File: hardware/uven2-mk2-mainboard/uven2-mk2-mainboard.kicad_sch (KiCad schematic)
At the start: 7 parts, among them U1 DEV-16771, U2 MCP48FEB28T-20E/ST, U3 MCP48FEB28T-20E/ST

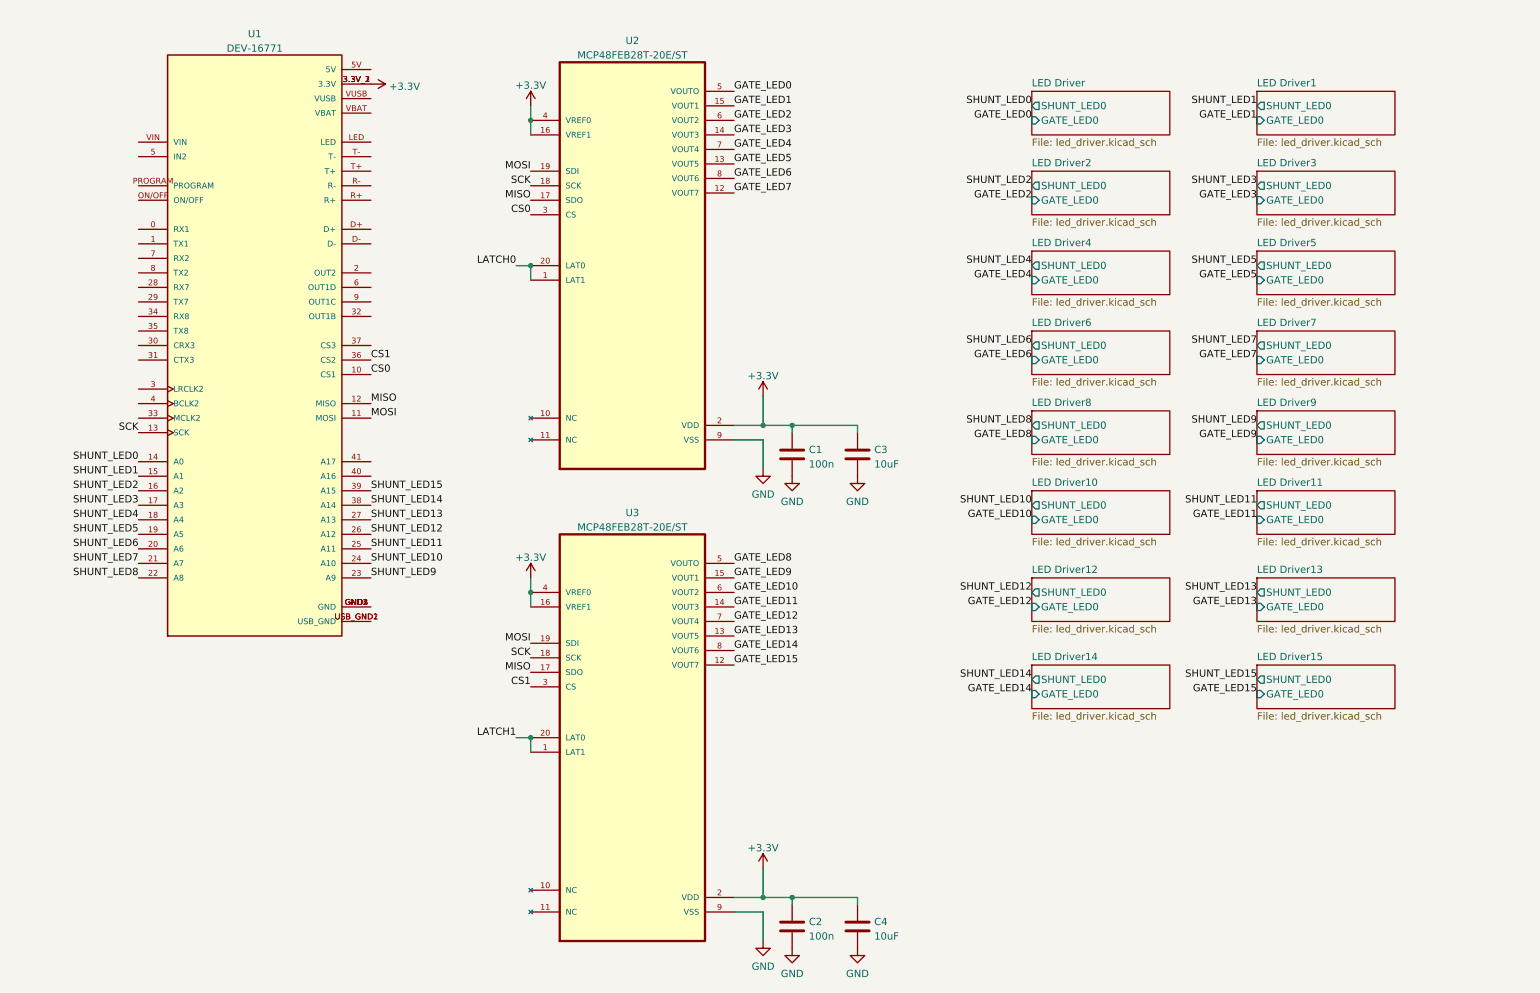
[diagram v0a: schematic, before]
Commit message: with current limiting switch
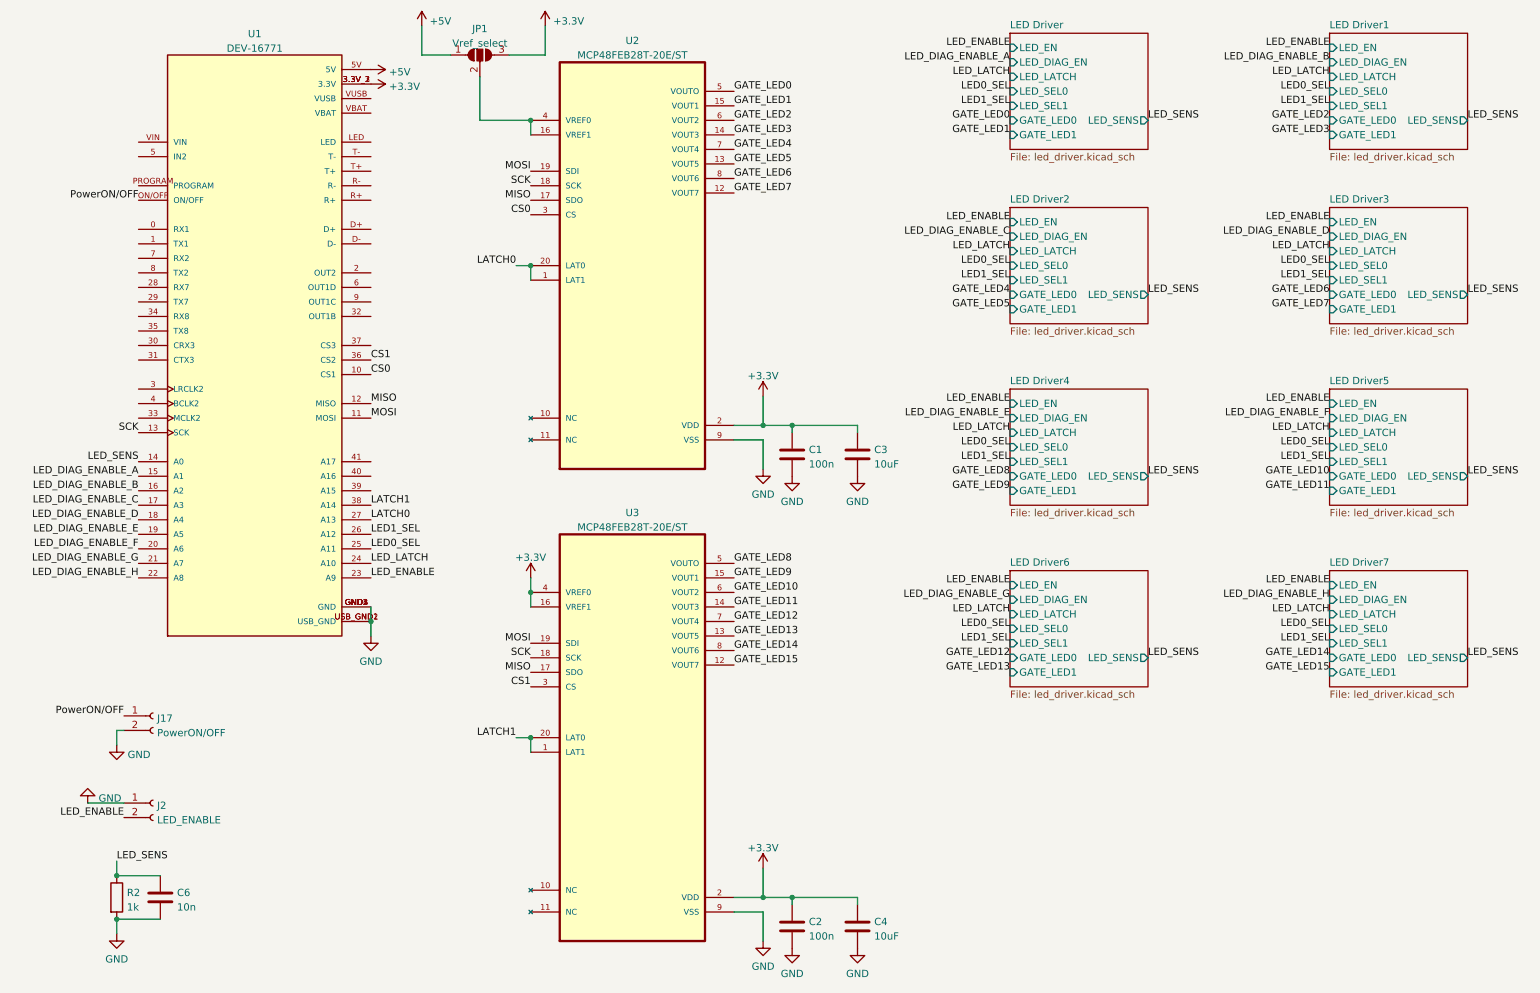
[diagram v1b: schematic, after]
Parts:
- added C6: 10n, Capacitor_SMD:C_0603_1608Metric_Pad1.08x0.95mm_HandSolder, symbol Device:C
- added J17: PowerON/OFF, Connector_PinHeader_2.54mm:PinHeader_1x02_P2.54mm_Vertical, symbol Connector:Conn_01x02_Female
- added J2: LED_ENABLE, Connector_PinHeader_2.54mm:PinHeader_1x02_P2.54mm_Vertical, symbol Connector:Conn_01x02_Female
- added JP1: Vref_select, Jumper:SolderJumper-3_P1.3mm_Open_RoundedPad1.0x1.5mm_NumberLabels, symbol Jumper:SolderJumper_3_Open
- added R2: 1k, Resistor_SMD:R_0603_1608Metric_Pad0.98x0.95mm_HandSolder, symbol Device:R
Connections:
- net SHUNT_LED13 is gone; now on net LATCH0: U1.27 (A13)
- net SHUNT_LED14 is gone; now on net LATCH1: U1.38 (A14)
- net +3.3V: now also JP1.3 (B); no longer U2.16 (VREF1), U2.4 (VREF0)
- net GND: now also U1.GND1 (GND), U1.GND2 (GND), U1.GND3 (GND), U1.GND4 (GND), U1.GND5 (GND), U1.USB_GND1 (USB_GND), U1.USB_GND2 (USB_GND), C6.2, J17.2 (Pin_2), J2.1 (Pin_1), R2.2
- net +5V: now reaches U1.5V
- net +5V: now also JP1.1 (A)
- net PowerON/OFF: now reaches U1.ON/OFF
- net PowerON/OFF: now also J17.1 (Pin_1)
- net SHUNT_LED0 renamed LED_SENS
- net LED_SENS: now also C6.1, R2.1
- net SHUNT_LED1 renamed LED_DIAG_ENABLE_A
- net SHUNT_LED10 renamed LED_LATCH
- net SHUNT_LED11 renamed LED0_SEL
- net SHUNT_LED12 renamed LED1_SEL
- net SHUNT_LED15: no longer names the net of U1.39 (A15)
- net SHUNT_LED2 renamed LED_DIAG_ENABLE_B
- net SHUNT_LED3 renamed LED_DIAG_ENABLE_C
- net SHUNT_LED4 renamed LED_DIAG_ENABLE_D
- net SHUNT_LED5 renamed LED_DIAG_ENABLE_E
- net SHUNT_LED6 renamed LED_DIAG_ENABLE_F
- net SHUNT_LED7 renamed LED_DIAG_ENABLE_G
- net SHUNT_LED8 renamed LED_DIAG_ENABLE_H
- net SHUNT_LED9 renamed LED_ENABLE
- net LED_ENABLE: now also J2.2 (Pin_2)
- new net: JP1.2 (C), U2.16 (VREF1), U2.4 (VREF0)
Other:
- removed sheet LED Driver10
- removed sheet LED Driver11
- removed sheet LED Driver12
- removed sheet LED Driver13
- removed sheet LED Driver14
- removed sheet LED Driver15
- removed sheet LED Driver8
- removed sheet LED Driver9
- sheet LED Driver ports: added GATE_LED1, LED_DIAG_EN, LED_EN, LED_LATCH, LED_SEL0, LED_SEL1, LED_SENS; removed SHUNT_LED0
- sheet LED Driver1 ports: added GATE_LED1, LED_DIAG_EN, LED_EN, LED_LATCH, LED_SEL0, LED_SEL1, LED_SENS; removed SHUNT_LED0
- sheet LED Driver2 ports: added GATE_LED1, LED_DIAG_EN, LED_EN, LED_LATCH, LED_SEL0, LED_SEL1, LED_SENS; removed SHUNT_LED0
- sheet LED Driver3 ports: added GATE_LED1, LED_DIAG_EN, LED_EN, LED_LATCH, LED_SEL0, LED_SEL1, LED_SENS; removed SHUNT_LED0
- sheet LED Driver4 ports: added GATE_LED1, LED_DIAG_EN, LED_EN, LED_LATCH, LED_SEL0, LED_SEL1, LED_SENS; removed SHUNT_LED0
- sheet LED Driver5 ports: added GATE_LED1, LED_DIAG_EN, LED_EN, LED_LATCH, LED_SEL0, LED_SEL1, LED_SENS; removed SHUNT_LED0
- sheet LED Driver6 ports: added GATE_LED1, LED_DIAG_EN, LED_EN, LED_LATCH, LED_SEL0, LED_SEL1, LED_SENS; removed SHUNT_LED0
- sheet LED Driver7 ports: added GATE_LED1, LED_DIAG_EN, LED_EN, LED_LATCH, LED_SEL0, LED_SEL1, LED_SENS; removed SHUNT_LED0

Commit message: with wago connector
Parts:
- added J1: 713-1436_037-000, custom_lib:CONN_713-1436&slash_037-000_WAG, symbol 713-1436_037-000:713-1436_037-000
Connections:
- net LATCH0: now also U1.6 (OUT1D); no longer U1.27 (A13)
- net LATCH1: now also U1.7 (RX2); no longer U1.38 (A14)
- net LED0_SEL: now also U1.4 (BCLK2); no longer U1.25 (A11)
- net LED1_SEL: now also U1.5 (IN2); no longer U1.26 (A12)
- net LED_DIAG_ENABLE_A: now also U1.8 (TX2); no longer U1.15 (A1)
- net LED_DIAG_ENABLE_B: now also U1.9 (OUT1C); no longer U1.16 (A2)
- net LED_DIAG_ENABLE_C: now also U1.28 (RX7); no longer U1.17 (A3)
- net LED_DIAG_ENABLE_D: now also U1.29 (TX7); no longer U1.18 (A4)
- net LED_DIAG_ENABLE_E: now also U1.30 (CRX3); no longer U1.19 (A5)
- net LED_DIAG_ENABLE_F: now also U1.31 (CTX3); no longer U1.20 (A6)
- net LED_DIAG_ENABLE_G: now also U1.33 (MCLK2); no longer U1.21 (A7)
- net LED_DIAG_ENABLE_H: now also U1.34 (RX8); no longer U1.22 (A8)
- net LED_ENABLE: now also U1.2 (OUT2); no longer U1.23 (A9)
- net LED_LATCH: now also U1.3 (LRCLK2); no longer U1.24 (A10)
- net TEMP_LED14: now reaches U1.39 (A15)
- net TEMP_LED15: now reaches U1.40 (A16)
- new net LED0+: J1.2
- new net LED0-: J1.1
- new net LED1+: J1.4
- new net LED1-: J1.3
- new net LED10+: J1.22
- new net LED10-: J1.21
- new net LED11+: J1.24
- new net LED11-: J1.23
- new net LED12+: J1.26
- new net LED12-: J1.25
- new net LED13+: J1.28
- new net LED13-: J1.27
- new net LED14+: J1.30
- new net LED14-: J1.29
- new net LED15+: J1.32
- new net LED15-: J1.31
- new net LED2+: J1.6
- new net LED2-: J1.5
- new net LED3+: J1.8
- new net LED3-: J1.7
- new net LED4+: J1.10
- new net LED4-: J1.9
- new net LED5+: J1.12
- new net LED5-: J1.11
- new net LED6+: J1.14
- new net LED6-: J1.13
- new net LED7+: J1.16
- new net LED7-: J1.15
- new net LED8+: J1.18
- new net LED8-: J1.17
- new net LED9+: J1.20
- new net LED9-: J1.19
- new net TEMP_LED0: U1.15 (A1)
- new net TEMP_LED1: U1.16 (A2)
- new net TEMP_LED10: U1.25 (A11)
- new net TEMP_LED11: U1.26 (A12)
- new net TEMP_LED12: U1.27 (A13)
- new net TEMP_LED13: U1.38 (A14)
- new net TEMP_LED2: U1.17 (A3)
- new net TEMP_LED3: U1.18 (A4)
- new net TEMP_LED4: U1.19 (A5)
- new net TEMP_LED5: U1.20 (A6)
- new net TEMP_LED6: U1.21 (A7)
- new net TEMP_LED7: U1.22 (A8)
- new net TEMP_LED8: U1.23 (A9)
- new net TEMP_LED9: U1.24 (A10)
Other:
- sheet LED Driver ports: added LED0+, LED0-, LED1+, LED1-, TEMP_LED0, TEMP_LED1; removed none
- sheet LED Driver1 ports: added LED0+, LED0-, LED1+, LED1-, TEMP_LED0, TEMP_LED1; removed none
- sheet LED Driver2 ports: added LED0+, LED0-, LED1+, LED1-, TEMP_LED0, TEMP_LED1; removed none
- sheet LED Driver3 ports: added LED0+, LED0-, LED1+, LED1-, TEMP_LED0, TEMP_LED1; removed none
- sheet LED Driver4 ports: added LED0+, LED0-, LED1+, LED1-, TEMP_LED0, TEMP_LED1; removed none
- sheet LED Driver5 ports: added LED0+, LED0-, LED1+, LED1-, TEMP_LED0, TEMP_LED1; removed none
- sheet LED Driver6 ports: added LED0+, LED0-, LED1+, LED1-, TEMP_LED0, TEMP_LED1; removed none
- sheet LED Driver7 ports: added LED0+, LED0-, LED1+, LED1-, TEMP_LED0, TEMP_LED1; removed none

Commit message: with chamber control
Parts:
- added C?: 100n, Capacitor_SMD:C_0603_1608Metric_Pad1.08x0.95mm_HandSolder, symbol Device:C
- added J?: J1B1211CCD, J1B1211CCD, symbol J1B1211CCD:J1B1211CCD
- added J? (x5): GND, symbol Connector:Conn_01x01_Female
- added J?: 28V, symbol Connector:Conn_01x01_Female
- added J? (x3): 24V, symbol Connector:Conn_01x01_Female
- added J?: 5V, symbol Connector:Conn_01x01_Female
- added J?: LED_CHAMBER_CONTROL, symbol Connector:DB25_Male_MountingHoles
- added JP?: Vref_select, Jumper:SolderJumper-3_P1.3mm_Open_RoundedPad1.0x1.5mm_NumberLabels, symbol Jumper:SolderJumper_3_Open
- added R? (x2): 1k, Resistor_SMD:R_0603_1608Metric_Pad0.98x0.95mm_HandSolder, symbol Device:R
- added U? (x2): G3VM-31DR_TR05_, symbol G3VM-31DR_TR05_:G3VM-31DR_TR05_
- J1: value 713-1436_037-000 -> LEDs
- U2, U3: footprint custom_lib:SOP65P640X120-20N -> SOP65P640X120-20N
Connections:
- net +3.3V: now also JP?.3 (B); no longer U3.16 (VREF1), U3.4 (VREF0)
- net +5V: now also J?.1 (Pin_1), JP?.1 (A)
- net CS0: now also U1.37 (CS3); no longer U1.10 (CS1)
- net GND: now also C?.2, J?.0 (PAD), J?.1 (Pin_1), J?.1 (Pin_1), J?.1 (Pin_1), J?.1 (Pin_1), J?.1 (Pin_1), J?.17 (P17), J?.19 (P19), J?.8 (RGND), J?.9 (KG), U?.2 (K), U?.2 (K), U?.4 (D), U?.4 (D)
- net LED_ENABLE: now also J?.18 (P18)
- net TEMP_LED0: now also J?.1
- net TEMP_LED1: now also J?.2
- net TEMP_LED10: now also J?.11
- net TEMP_LED11: now also J?.12
- net TEMP_LED12: now also J?.13
- net TEMP_LED13: now also J?.14 (P14)
- net TEMP_LED14: now also J?.15 (P15)
- net TEMP_LED15: now also J?.16 (P16)
- net TEMP_LED2: now also J?.3
- net TEMP_LED3: now also J?.4
- net TEMP_LED4: now also J?.5
- net TEMP_LED5: now also J?.6
- net TEMP_LED6: now also J?.7
- net TEMP_LED7: now also J?.8
- net TEMP_LED8: now also J?.9
- net TEMP_LED9: now also J?.10
- net at U3.10 (NC): now also U3.11 (NC)
- net LED_FAN: now reaches U1.41 (A17)
- net LED_FAN: now also R?.1
- net ETH_LED: now reaches U1.LED
- net ETH_LED: now also J?.10 (AG)
- net ETH_RX+: now reaches U1.R+
- net ETH_RX+: now also J?.4 (RD+)
- net ETH_RX-: now reaches U1.R-
- net ETH_RX-: now also J?.6 (RD-)
- net ETH_TX+: now reaches U1.T+
- net ETH_TX+: now also J?.1 (TD+)
- net ETH_TX-: now reaches U1.T-
- net ETH_TX-: now also J?.3 (TD-)
- net at U2.10 (NC): now also U2.11 (NC)
- new net: C?.1, J?.2 (TCT), J?.5 (RCT)
- new net: R?.2, U?.1 (A) (x2)
- new net: J?.22 (P22), J?.23 (P23), U?.3 (D2)
- new net: JP?.2 (C), U3.16 (VREF1), U3.4 (VREF0)
- new net: J?.20 (P20), U?.3 (D2)
- new net +24V: J?.1 (Pin_1), J?.1 (Pin_1), J?.1 (Pin_1)
- new net +28V: J?.1 (Pin_1), J?.21 (P21), J?.24 (P24), J?.25 (P25)
- new net CHAMBER_FAN: R?.1
- no-connect marks 0 -> 5
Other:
- moved on the sheet: C1, C2, C3, C4, C6, J1, J17, J2, JP1, R2

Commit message: schematics done
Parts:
- removed J2: LED_ENABLE, Connector_PinHeader_2.54mm:PinHeader_1x02_P2.54mm_Vertical, symbol Connector:Conn_01x02_Female
- removed J? (x2): GND, symbol Connector:Conn_01x01_Female
- removed J?: 28V, symbol Connector:Conn_01x01_Female
- removed J?: 5V, symbol Connector:Conn_01x01_Female
- removed J?: LED_CHAMBER_CONTROL, symbol Connector:DB25_Male_MountingHoles
- removed R? (x2): 1k, Resistor_SMD:R_0603_1608Metric_Pad0.98x0.95mm_HandSolder, symbol Device:R
- removed U? (x2): G3VM-31DR_TR05_, symbol G3VM-31DR_TR05_:G3VM-31DR_TR05_
- added J15: Chamber_Control, Connector_Dsub:DSUB-37_Female_Horizontal_P2.77x2.84mm_EdgePinOffset7.70mm_Housed_MountingHolesOffset9.12mm, symbol Connector:DB37_Male_MountingHoles
- added J2: 1-282834-0, custom_lib:TE_1-282834-0, symbol 1-282834-0:1-282834-0
- added J3: 5V, custom_lib:KEYSTONE_7767, symbol 7767:7767
- added J4, J7: GND, custom_lib:KEYSTONE_7767, symbol 7767:7767
- added J6: 24V, custom_lib:KEYSTONE_7767, symbol 7767:7767
- added J8: USB_HOST, Connector_PinHeader_2.54mm:PinHeader_1x05_P2.54mm_Vertical, symbol Connector:Conn_01x05_Male
- added Q1, Q2: 2N7002, Package_TO_SOT_SMD:SOT-23, symbol Transistor_FET:2N7002
- added R50: 1k, Resistor_SMD:R_0603_1608Metric_Pad0.98x0.95mm_HandSolder, symbol Device:R
- added R51, R52: 10k, Resistor_SMD:R_0603_1608Metric_Pad0.98x0.95mm_HandSolder, symbol Device:R
- added TP1: 5V, custom_lib:TP420X150, symbol RCWCTE:RCWCTE
- added TP10: LED_DIAG_ENABLE_E, custom_lib:TP420X150, symbol RCWCTE:RCWCTE
- added TP11: LED_DIAG_ENABLE_F, custom_lib:TP420X150, symbol RCWCTE:RCWCTE
- added TP12: LED_LATCH, custom_lib:TP420X150, symbol RCWCTE:RCWCTE
- added TP13: LED0_SEL, custom_lib:TP420X150, symbol RCWCTE:RCWCTE
- added TP14: LED_DIAG_ENABLE_G, custom_lib:TP420X150, symbol RCWCTE:RCWCTE
- added TP15: SCK, custom_lib:TP420X150, symbol RCWCTE:RCWCTE
- added TP16: LED_SENS, custom_lib:TP420X150, symbol RCWCTE:RCWCTE
- added TP17: TEMP_LED0, custom_lib:TP420X150, symbol RCWCTE:RCWCTE
- added TP18: TEMP_LED1, custom_lib:TP420X150, symbol RCWCTE:RCWCTE
- added TP19: TEMP_LED2, custom_lib:TP420X150, symbol RCWCTE:RCWCTE
- added TP2, TP26, TP28: GND, custom_lib:TP420X150, symbol RCWCTE:RCWCTE
- added TP20: TEMP_LED3, custom_lib:TP420X150, symbol RCWCTE:RCWCTE
- added TP21: TEMP_LED4, custom_lib:TP420X150, symbol RCWCTE:RCWCTE
- added TP22: TEMP_LED5, custom_lib:TP420X150, symbol RCWCTE:RCWCTE
- added TP23: TEMP_LED6, custom_lib:TP420X150, symbol RCWCTE:RCWCTE
- added TP24: TEMP_LED7, custom_lib:TP420X150, symbol RCWCTE:RCWCTE
- added TP25: 24V_FANS, custom_lib:TP420X150, symbol RCWCTE:RCWCTE
- added TP27: 24V_LEDS, custom_lib:TP420X150, symbol RCWCTE:RCWCTE
- added TP29: LED_ENABLE, custom_lib:TP420X150, symbol RCWCTE:RCWCTE
- added TP3: LED1_SEL, custom_lib:TP420X150, symbol RCWCTE:RCWCTE
- added TP30: LATCH0, custom_lib:TP420X150, symbol RCWCTE:RCWCTE
- added TP31: LED_DIAG_ENABLE_B, custom_lib:TP420X150, symbol RCWCTE:RCWCTE
- added TP32: LED_DIAG_ENABLE_D, custom_lib:TP420X150, symbol RCWCTE:RCWCTE
- added TP33: CS0, custom_lib:TP420X150, symbol RCWCTE:RCWCTE
- added TP34: CS1, custom_lib:TP420X150, symbol RCWCTE:RCWCTE
- added TP35: MISO, custom_lib:TP420X150, symbol RCWCTE:RCWCTE
- added TP36: MOSI, custom_lib:TP420X150, symbol RCWCTE:RCWCTE
- added TP37: LED_DIAG_ENABLE_C, custom_lib:TP420X150, symbol RCWCTE:RCWCTE
- added TP38: TEMP_LED15, custom_lib:TP420X150, symbol RCWCTE:RCWCTE
- added TP39: TEMP_LED14, custom_lib:TP420X150, symbol RCWCTE:RCWCTE
- added TP4: PowerON/OFF, custom_lib:TP420X150, symbol RCWCTE:RCWCTE
- added TP40: TEMP_LED13, custom_lib:TP420X150, symbol RCWCTE:RCWCTE
- added TP41: TEMP_LED12, custom_lib:TP420X150, symbol RCWCTE:RCWCTE
- added TP42: TEMP_LED11, custom_lib:TP420X150, symbol RCWCTE:RCWCTE
- added TP43: TEMP_LED10, custom_lib:TP420X150, symbol RCWCTE:RCWCTE
- added TP44: TEMP_LED9, custom_lib:TP420X150, symbol RCWCTE:RCWCTE
- added TP45: TEMP_LED8, custom_lib:TP420X150, symbol RCWCTE:RCWCTE
- added TP46: GATE_LED0, custom_lib:TP420X150, symbol RCWCTE:RCWCTE
- added TP47: GATE_LED1, custom_lib:TP420X150, symbol RCWCTE:RCWCTE
- added TP48: GATE_LED2, custom_lib:TP420X150, symbol RCWCTE:RCWCTE
- added TP49: GATE_LED3, custom_lib:TP420X150, symbol RCWCTE:RCWCTE
- added TP5: LATCH1, custom_lib:TP420X150, symbol RCWCTE:RCWCTE
- added TP50: GATE_LED4, custom_lib:TP420X150, symbol RCWCTE:RCWCTE
- added TP51: GATE_LED5, custom_lib:TP420X150, symbol RCWCTE:RCWCTE
- added TP52: GATE_LED6, custom_lib:TP420X150, symbol RCWCTE:RCWCTE
- added TP53: GATE_LED7, custom_lib:TP420X150, symbol RCWCTE:RCWCTE
- added TP54: GATE_LED8, custom_lib:TP420X150, symbol RCWCTE:RCWCTE
- added TP55: GATE_LED9, custom_lib:TP420X150, symbol RCWCTE:RCWCTE
- added TP56: GATE_LED10, custom_lib:TP420X150, symbol RCWCTE:RCWCTE
- added TP57: GATE_LED11, custom_lib:TP420X150, symbol RCWCTE:RCWCTE
- added TP58: GATE_LED12, custom_lib:TP420X150, symbol RCWCTE:RCWCTE
- added TP59: GATE_LED13, custom_lib:TP420X150, symbol RCWCTE:RCWCTE
- added TP6: LED_DIAG_ENABLE_A, custom_lib:TP420X150, symbol RCWCTE:RCWCTE
- added TP60: GATE_LED14, custom_lib:TP420X150, symbol RCWCTE:RCWCTE
- added TP61: GATE_LED15, custom_lib:TP420X150, symbol RCWCTE:RCWCTE
- added TP62: LED15+, custom_lib:TP420X150, symbol RCWCTE:RCWCTE
- added TP63: LED15-, custom_lib:TP420X150, symbol RCWCTE:RCWCTE
- added TP64: LED14+, custom_lib:TP420X150, symbol RCWCTE:RCWCTE
- added TP65: LED14-, custom_lib:TP420X150, symbol RCWCTE:RCWCTE
- added TP66: LED13+, custom_lib:TP420X150, symbol RCWCTE:RCWCTE
- added TP67: LED13-, custom_lib:TP420X150, symbol RCWCTE:RCWCTE
- added TP68: LED12+, custom_lib:TP420X150, symbol RCWCTE:RCWCTE
- added TP69: LED12-, custom_lib:TP420X150, symbol RCWCTE:RCWCTE
- added TP7: LED_FAN, custom_lib:TP420X150, symbol RCWCTE:RCWCTE
- added TP70: LED11+, custom_lib:TP420X150, symbol RCWCTE:RCWCTE
- added TP71: LED11-, custom_lib:TP420X150, symbol RCWCTE:RCWCTE
- added TP72: LED10+, custom_lib:TP420X150, symbol RCWCTE:RCWCTE
- added TP73: LED10-, custom_lib:TP420X150, symbol RCWCTE:RCWCTE
- added TP74: LED9+, custom_lib:TP420X150, symbol RCWCTE:RCWCTE
- added TP75: LED9-, custom_lib:TP420X150, symbol RCWCTE:RCWCTE
- added TP76: LED8+, custom_lib:TP420X150, symbol RCWCTE:RCWCTE
- added TP77: LED8-, custom_lib:TP420X150, symbol RCWCTE:RCWCTE
- added TP78: LED7+, custom_lib:TP420X150, symbol RCWCTE:RCWCTE
- added TP79: LED7-, custom_lib:TP420X150, symbol RCWCTE:RCWCTE
- added TP8: CHAMBER_FAN, custom_lib:TP420X150, symbol RCWCTE:RCWCTE
- added TP80: LED6+, custom_lib:TP420X150, symbol RCWCTE:RCWCTE
- added TP81: LED6-, custom_lib:TP420X150, symbol RCWCTE:RCWCTE
- added TP82: LED5+, custom_lib:TP420X150, symbol RCWCTE:RCWCTE
- added TP83: LED5-, custom_lib:TP420X150, symbol RCWCTE:RCWCTE
- added TP84: LED4+, custom_lib:TP420X150, symbol RCWCTE:RCWCTE
- added TP85: LED4-, custom_lib:TP420X150, symbol RCWCTE:RCWCTE
- added TP86: LED3+, custom_lib:TP420X150, symbol RCWCTE:RCWCTE
- added TP87: LED3-, custom_lib:TP420X150, symbol RCWCTE:RCWCTE
- added TP88: LED2+, custom_lib:TP420X150, symbol RCWCTE:RCWCTE
- added TP89: LED2-, custom_lib:TP420X150, symbol RCWCTE:RCWCTE
- added TP9: LED_DIAG_ENABLE_H, custom_lib:TP420X150, symbol RCWCTE:RCWCTE
- added TP90: LED1+, custom_lib:TP420X150, symbol RCWCTE:RCWCTE
- added TP91: LED1-, custom_lib:TP420X150, symbol RCWCTE:RCWCTE
- added TP92: LED0+, custom_lib:TP420X150, symbol RCWCTE:RCWCTE
- added TP93: LED0-, custom_lib:TP420X150, symbol RCWCTE:RCWCTE
- J10, J11, J12, J13, J14, J9: renamed from J?; footprint (none) -> custom_lib:7466205R
- J5: renamed from J?; footprint J1B1211CCD -> custom_lib:J1B1211CCD
- U2, U3: footprint SOP65P640X120-20N -> custom_lib:SOP65P640X120-20N
- gave numbers to parts that had none: 2
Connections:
- net +24V: now also J15.20, J15.21, J15.22, J15.23, J15.24, J15.25, J15.26, J15.27, J2.8, J6.1, J6.2, J6.3, J6.4, TP25.1, TP27.1
- net +5V: now also U1.VIN, J2.10, J3.1, J3.2, J3.3, J3.4, J8.1 (Pin_1), R51.1, R52.1, TP1.1; no longer U1.5V
- net CHAMBER_FAN: now also U1.29 (TX7), Q2.1 (G), TP8.1
- net CS0: now also TP33.1
- net CS1: now also TP34.1
- net GATE_LED0: now also TP46.1
- net GATE_LED1: now also TP47.1
- net GATE_LED10: now also TP56.1
- net GATE_LED11: now also TP57.1
- net GATE_LED12: now also TP58.1
- net GATE_LED13: now also TP59.1
- net GATE_LED14: now also TP60.1
- net GATE_LED15: now also TP61.1
- net GATE_LED2: now also TP48.1
- net GATE_LED3: now also TP49.1
- net GATE_LED4: now also TP50.1
- net GATE_LED5: now also TP51.1
- net GATE_LED6: now also TP52.1
- net GATE_LED7: now also TP53.1
- net GATE_LED8: now also TP54.1
- net GATE_LED9: now also TP55.1
- net GND: now also J15.0 (PAD), J15.18, J15.19, J15.29, J15.30, J15.31, J15.32, J15.33, J15.34, J15.35, J2.1, J2.3, J2.6, J2.7, J2.9, J4.1, J4.2, J4.3, J4.4, J7.1, J7.2, J7.3, J7.4, J8.4 (Pin_4), J8.5 (Pin_5), Q1.2 (S), Q2.2 (S), TP2.1, TP26.1, TP28.1; no longer J17.2 (Pin_2)
- net LATCH0: now also TP30.1
- net LATCH1: now also TP5.1
- net LED0+: now also TP92.1
- net LED0-: now also TP93.1
- net LED0_SEL: now also TP13.1
- net LED1+: now also TP90.1
- net LED1-: now also TP91.1
- net LED10+: now also TP72.1
- net LED10-: now also TP73.1
- net LED11+: now also TP70.1
- net LED11-: now also TP71.1
- net LED12+: now also TP68.1
- net LED12-: now also TP69.1
- net LED13+: now also TP66.1
- net LED13-: now also TP67.1
- net LED14+: now also TP64.1
- net LED14-: now also TP65.1
- net LED15+: now also TP62.1
- net LED15-: now also TP63.1
- net LED1_SEL: now also TP3.1
- net LED2+: now also TP88.1
- net LED2-: now also TP89.1
- net LED3+: now also TP86.1
- net LED3-: now also TP87.1
- net LED4+: now also TP84.1
- net LED4-: now also TP85.1
- net LED5+: now also TP82.1
- net LED5-: now also TP83.1
- net LED6+: now also TP80.1
- net LED6-: now also TP81.1
- net LED7+: now also TP78.1
- net LED7-: now also TP79.1
- net LED8+: now also TP76.1
- net LED8-: now also TP77.1
- net LED9+: now also TP74.1
- net LED9-: now also TP75.1
- net LED_DIAG_ENABLE_A: now also TP6.1
- net LED_DIAG_ENABLE_B: now also TP31.1
- net LED_DIAG_ENABLE_C: now also U1.41 (A17), TP37.1; no longer U1.28 (RX7)
- net LED_DIAG_ENABLE_D: now also U1.32 (OUT1B), TP32.1; no longer U1.29 (TX7)
- net LED_DIAG_ENABLE_E: now also TP10.1
- net LED_DIAG_ENABLE_F: now also TP11.1
- net LED_DIAG_ENABLE_G: now also TP14.1
- net LED_DIAG_ENABLE_H: now also TP9.1
- net LED_ENABLE: now also J15.17, J15.28, J2.2, R50.2, TP29.1; no longer U1.2 (OUT2)
- net LED_FAN: now also U1.28 (RX7), Q1.1 (G), TP7.1; no longer U1.41 (A17)
- net LED_LATCH: now also TP12.1
- net LED_SENS: now also TP16.1
- net MISO: now also TP35.1
- net MOSI: now also TP36.1
- net PowerON/OFF: now also J2.4, TP4.1
- net SCK: now also TP15.1
- net TEMP_LED0: now also J15.1, TP17.1
- net TEMP_LED1: now also J15.2, TP18.1
- net TEMP_LED10: now also J15.11, TP43.1
- net TEMP_LED11: now also J15.12, TP42.1
- net TEMP_LED12: now also J15.13, TP41.1
- net TEMP_LED13: now also J15.14, TP40.1
- net TEMP_LED14: now also J15.15, TP39.1
- net TEMP_LED15: now also J15.16, TP38.1
- net TEMP_LED2: now also J15.3, TP19.1
- net TEMP_LED3: now also J15.4, TP20.1
- net TEMP_LED4: now also J15.5, TP21.1
- net TEMP_LED5: now also J15.6, TP22.1
- net TEMP_LED6: now also J15.7, TP23.1
- net TEMP_LED7: now also J15.8, TP24.1
- net TEMP_LED8: now also J15.9, TP45.1
- net TEMP_LED9: now also J15.10, TP44.1
- net GPIO_0: now reaches U1.35 (TX8)
- net GPIO_0: now also J2.5
- net USB_HOST_D+: now reaches U1.D+
- net USB_HOST_D+: now also J8.3 (Pin_3)
- net USB_HOST_D-: now reaches U1.D-
- net USB_HOST_D-: now also J8.2 (Pin_2)
- new net: J15.36, Q1.3 (D), R51.2
- new net: J15.37, Q2.3 (D), R52.2
- new net: R50.1, U1.2 (OUT2)
- no-connect marks 5 -> 12
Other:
- moved on the sheet: C1, C2, C3, C38, C4, C6, J1, J10, J11, J12, J13, J14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
